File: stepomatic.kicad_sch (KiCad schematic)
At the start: 33 parts, among them J1 I2C, J4 USB_B_Micro, Q1 MMBT3904, Q2 MMBT3904, SW1 Mode, SW2 RST, U1 HDC1080DMBR, U3 ULN2003A, U4 CH340C, U5 28BYJ-48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

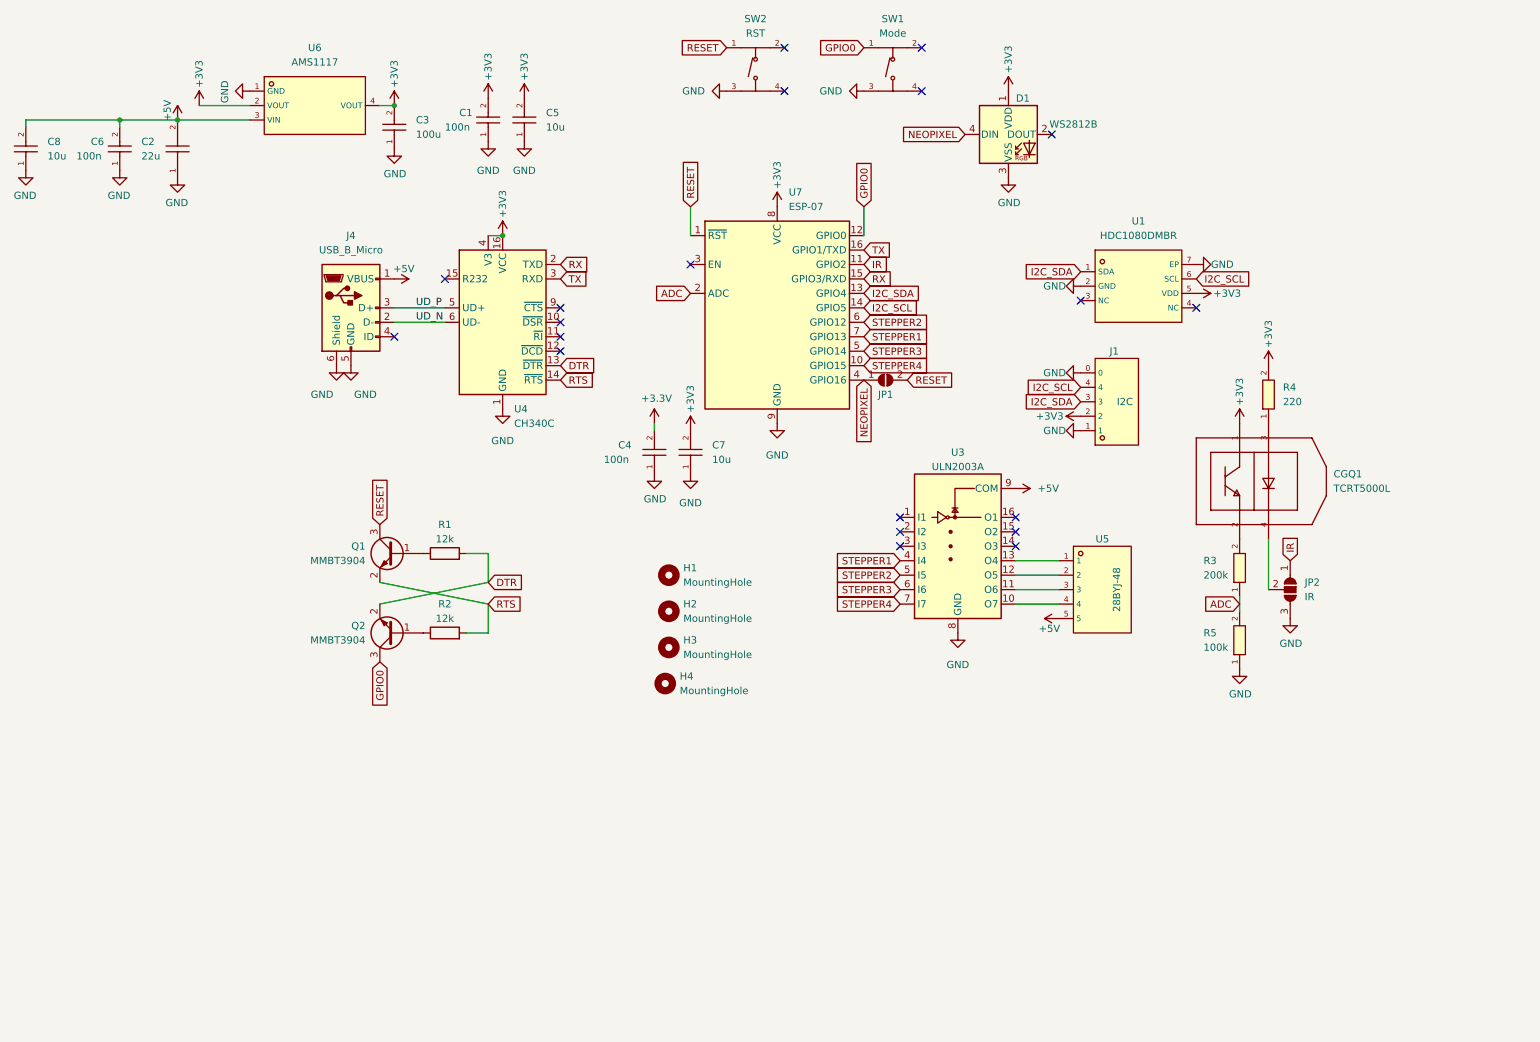
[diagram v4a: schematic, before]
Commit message: Add oshw logo, silkscreen improvements capacitor for adc
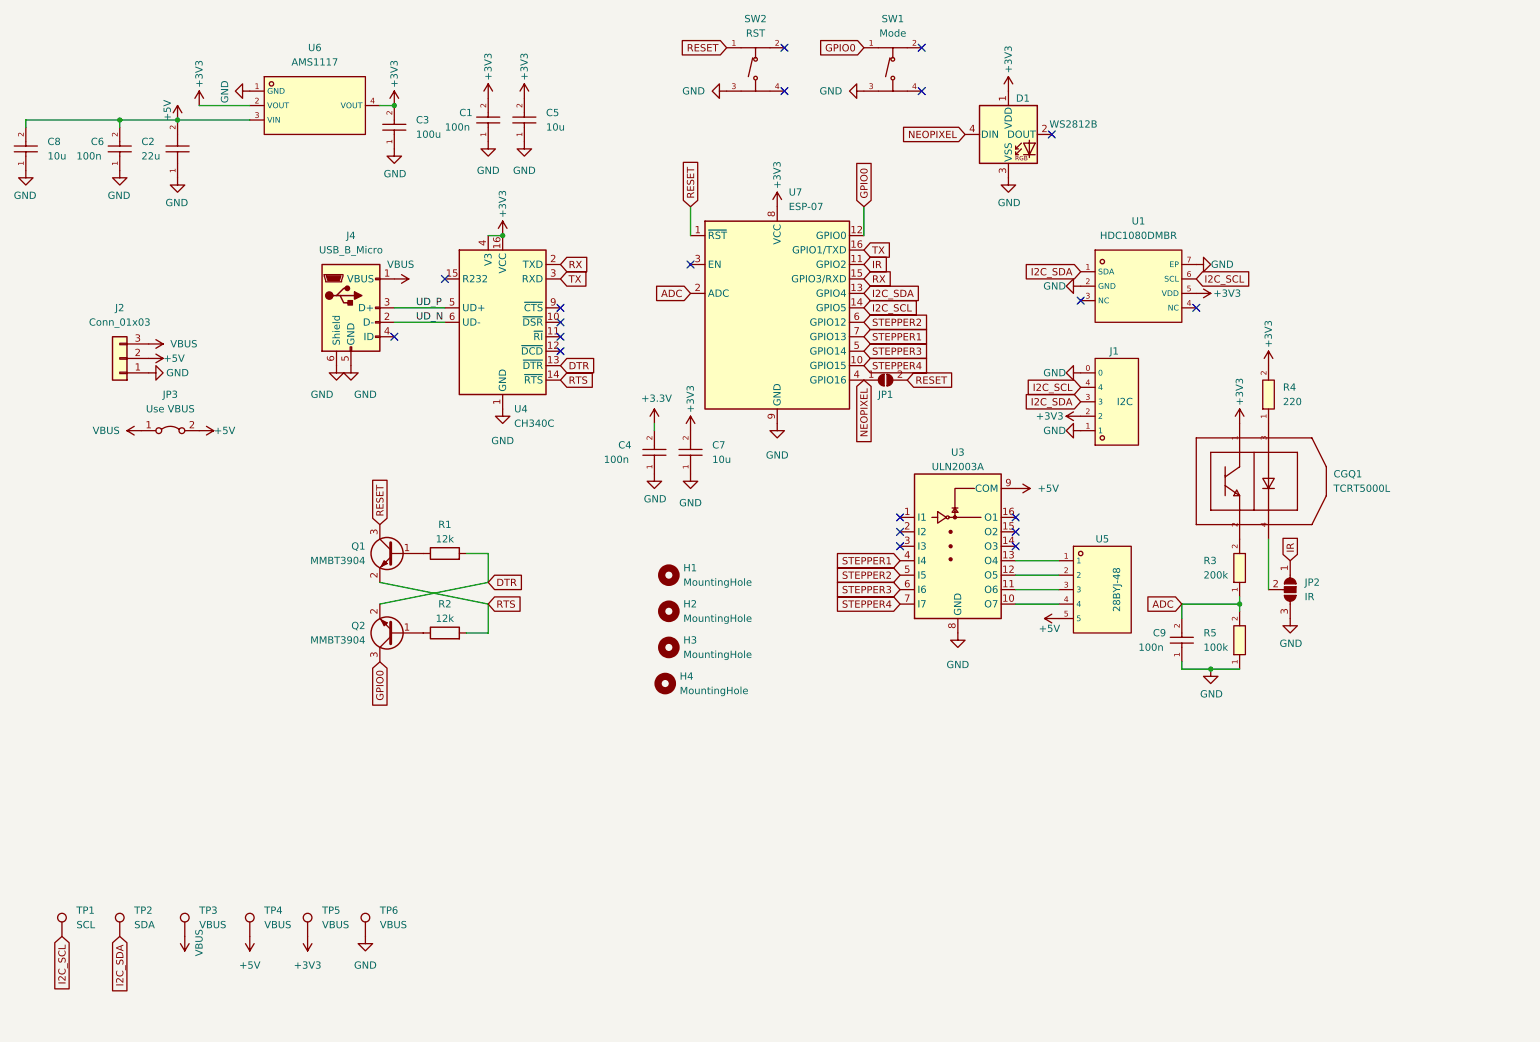
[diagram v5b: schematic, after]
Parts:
- added C9: 100n, footprint:C0402, symbol CL05B104KO5NNNC:CL05B104KO5NNNC
- added J2: Conn_01x03, Connector_PinHeader_2.54mm:PinHeader_1x03_P2.54mm_Vertical_SMD_Pin1Left, symbol Connector_Generic:Conn_01x03
- added JP3: Use VBUS, Jumper:SolderJumper-2_P1.3mm_Bridged2Bar_RoundedPad1.0x1.5mm, symbol Jumper:Jumper_2_Bridged
- added TP1: SCL, TestPoint:TestPoint_Pad_D1.0mm, symbol Connector:TestPoint
- added TP2: SDA, TestPoint:TestPoint_Pad_D1.0mm, symbol Connector:TestPoint
- added TP3, TP4, TP5, TP6: VBUS, TestPoint:TestPoint_Pad_D1.0mm, symbol Connector:TestPoint
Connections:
- net +3V3: now also TP5.1
- net +5V: now also J2.2 (Pin_2), JP3.2 (B), TP4.1; no longer J4.1 (VBUS)
- net ADC: now also C9.2
- net GND: now also C9.1, J2.1 (Pin_1), TP6.1
- net I2C_SCL: now also TP1.1
- net I2C_SDA: now also TP2.1
- new net VBUS: J2.3 (Pin_3), J4.1 (VBUS), JP3.1 (A), TP3.1

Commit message: Prettify schematic
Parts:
- J2: value Conn_01x03 -> 5V Switch
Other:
- note added: "Motor"
- note added: "POWER"
- note added: "Peripherals"
- note added: "SOC"
- note added: "Testpoints + Mounting Holes"
- note added: "USB + UART"
- moved on the sheet: C1, C2, C3, C4, C5, C6, C7, C8, C9, CGQ1, D1, H1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

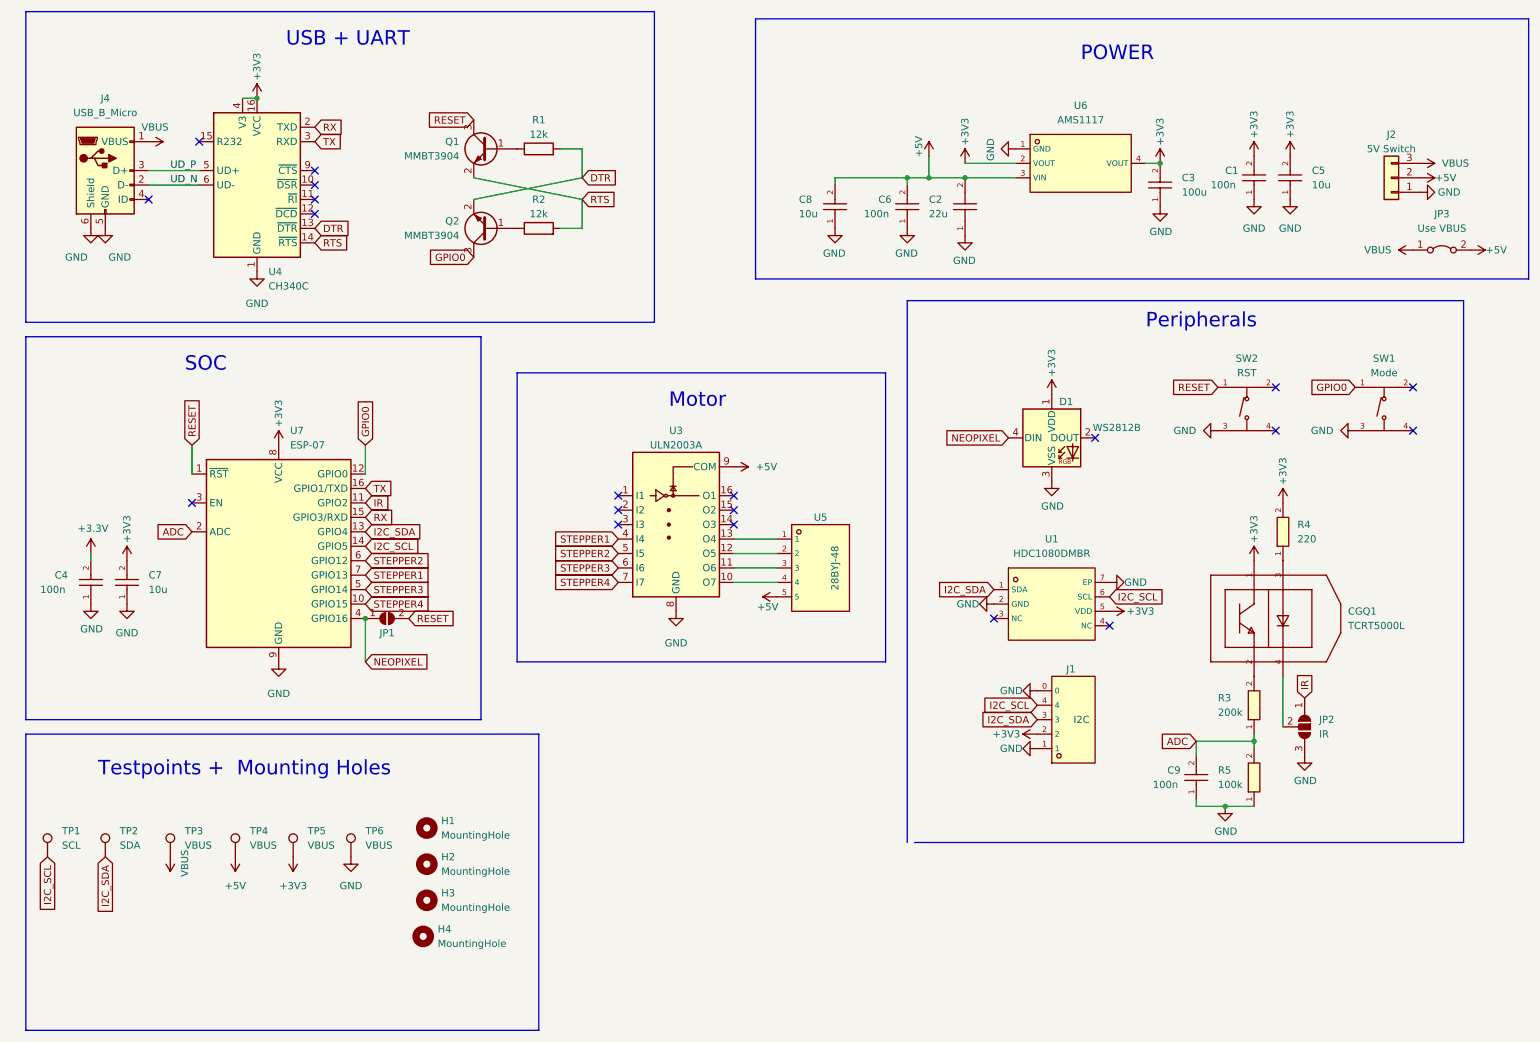
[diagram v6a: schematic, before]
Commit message: Exclude unpopulatable components from BOM
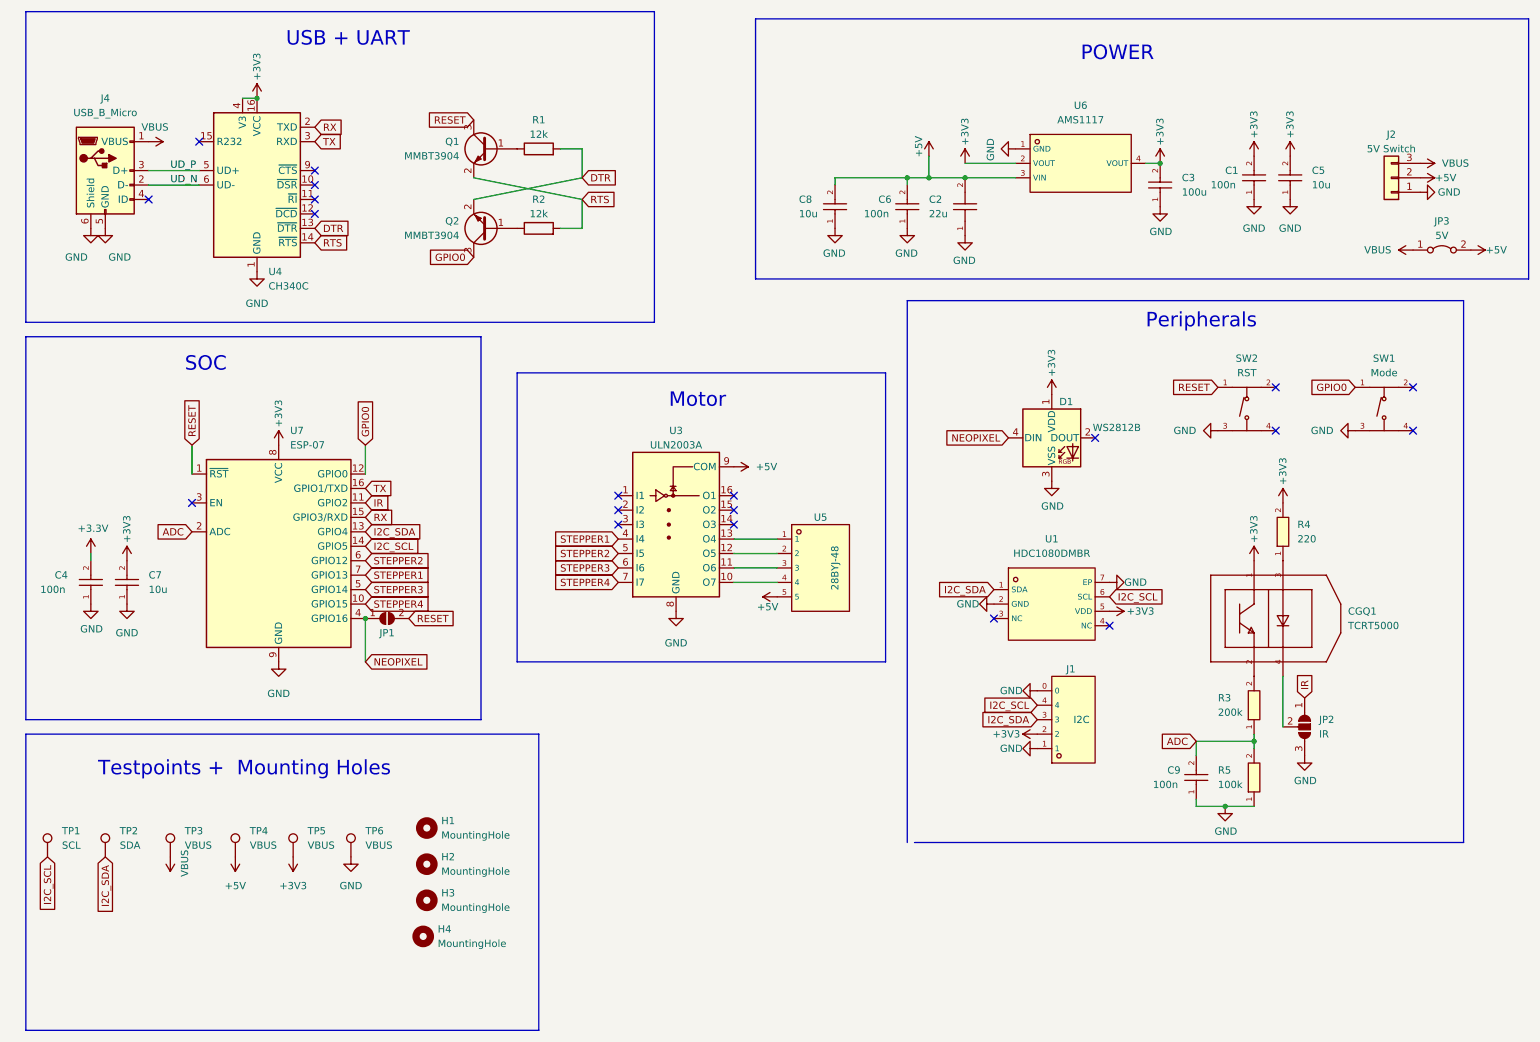
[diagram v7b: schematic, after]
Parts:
- CGQ1: value TCRT5000L -> TCRT5000
- JP2, TP1, TP2, TP3, TP4, TP5, TP6: now left out of the parts list
- JP3: value Use VBUS -> 5V; now left out of the parts list
